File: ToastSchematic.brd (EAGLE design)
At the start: 90 x 75 mm, 83 parts, among them Q1 DMN63D8LDW, Q2 DMN63D8LDW, Q3 DMN63D8LDW, Q4 DMN63D8LDW, T1 BPX81, T2 BPX81, T3 BPX81, T4 BPX81, T5 BPX81, T6 BPX81, U3 DRV8839_DSS_12, U4 DRV8839_DSS_12

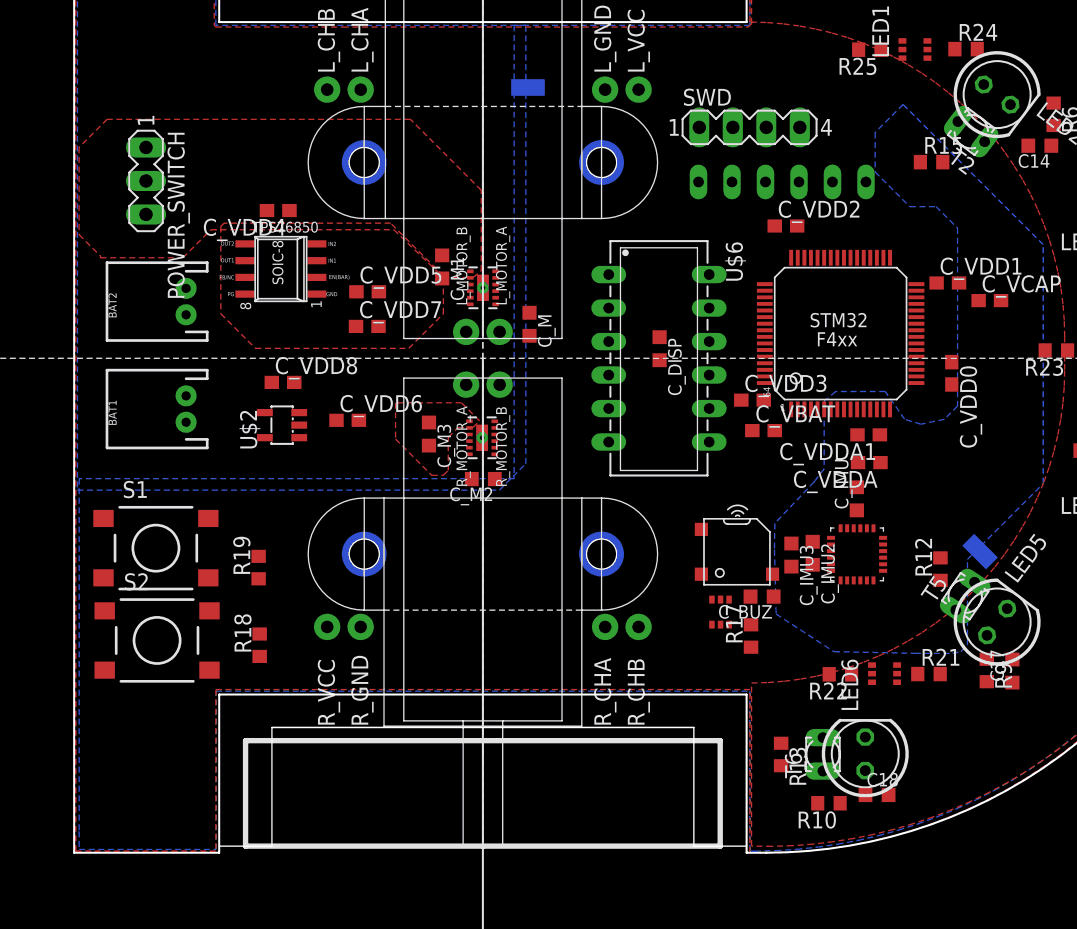
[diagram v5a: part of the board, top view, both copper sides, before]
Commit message: Added Ground Splitter
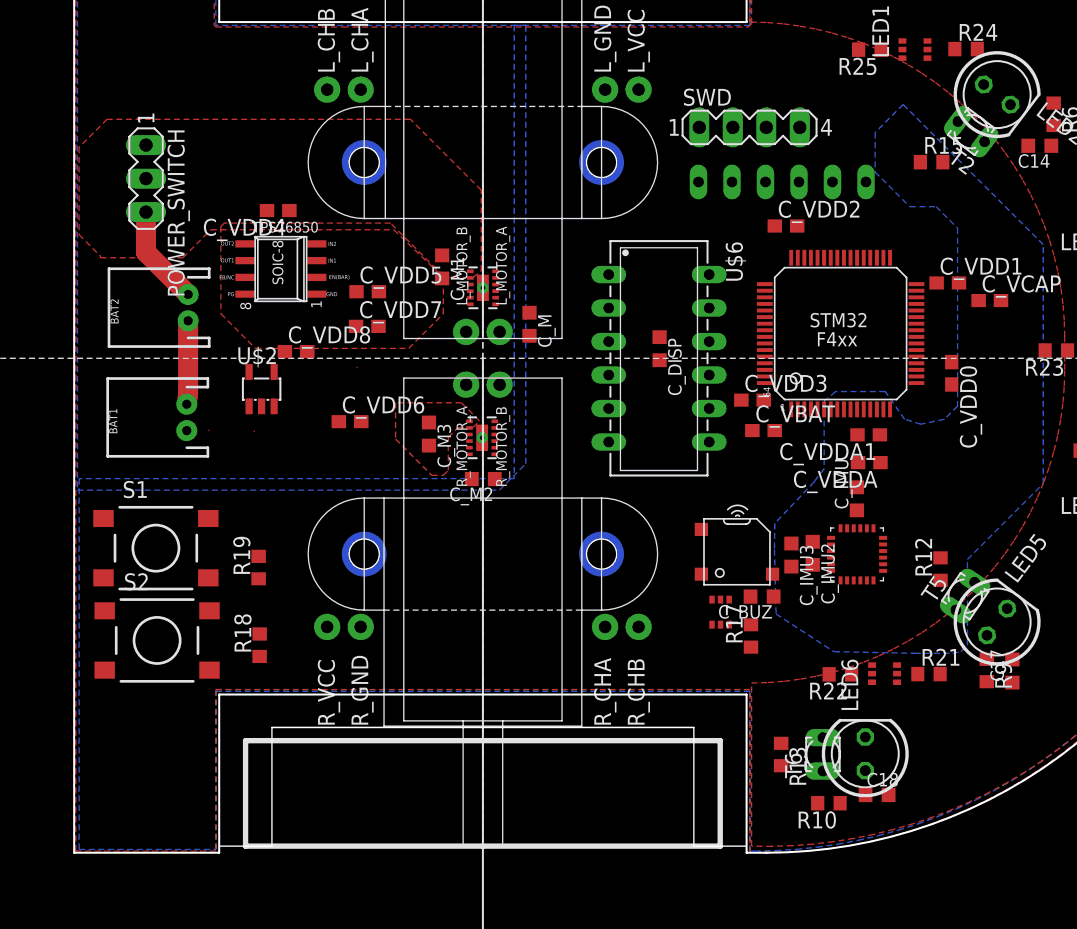
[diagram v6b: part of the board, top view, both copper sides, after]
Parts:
- removed SH1, SH2: SHORT-HT5, shorts-old:SHORT_TOP-50
- added U$5, U$8, U$9: SPLITTER, splitter:SPLITTER
- moved U$2 3.14 mm to (14.2, 35.2), turned to 0 degrees
- moved C_VDD8 2.54 mm to (16.8, 38.0)
- moved BAT1 0.64 mm to (8.54, 33.0)
- moved BAT2 0.48 mm to (8.64, 41.3)
- moved C_VDD6 0.20 mm to (20.9, 32.7)
- moved POWER_SWITCH 0.18 mm to (5.45, 51.1)
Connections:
- new net MGND: C_M.2, C_M2.2, U$9.2
- net AGND: now also U$8.2; no longer SH2.2
- net DGND: now also U$5.2; no longer SH1.2, SH2.1
- net GND: now also U$5.1, U$8.1, U$9.1; no longer C_M.2, C_M2.2, SH1.1
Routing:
- net N$2: track 0.00 -> 7.57 mm
- net N$1: track 0.00 -> 6.33 mm

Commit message: Get everything on cheap week
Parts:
- moved U$9 10.1 mm to (11.7, 34.5)
- moved R18 7.19 mm to (16.7, 22.4), turned to 270 degrees
- moved U$5 7.19 mm to (5.03, 37.0)
- moved C17 7.05 mm to (64.2, 12.5)
- moved U4 6.76 mm to (37.1, 40.0), turned to 180 degrees
- moved S1 6.40 mm to (7.38, 29.4), turned to 90 degrees
- moved U$8 5.25 mm to (12.2, 37.0)
- moved BAT1 5.06 mm to (7.78, 38.0)
- moved BAT2 4.22 mm to (7.70, 45.5)
- moved POWER_SWITCH 3.66 mm to (5.35, 54.8)
- moved S2 3.42 mm to (7.73, 19.2), turned to 180 degrees
- moved U$2 3.21 mm to (17.2, 36.4)
- moved R19 2.55 mm to (14.2, 24.2)
- moved C_IMU3 2.13 mm to (54.4, 24.7)
- moved R21 2.01 mm to (64.7, 15.6)
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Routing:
- net DGND: track 0.00 -> 245.6 mm
- net NRST: track 0.00 -> 72.8 mm, vias 0 -> 2
- net AGND: track 0.00 -> 64.4 mm, vias 0 -> 3
- net L_ENC_A: track 0.00 -> 37.0 mm
- net BUZZER: track 0.00 -> 31.6 mm, vias 0 -> 2
- net SCK: track 0.00 -> 29.3 mm
- net SWCLK: track 0.00 -> 28.3 mm
- net MGND: track 0.00 -> 27.9 mm
- net SWDIO: track 0.00 -> 21.9 mm, vias 0 -> 2
- net IR_DR: track 0.00 -> 20.2 mm
- net MOSI: track 0.00 -> 19.8 mm
- net IR_FR: track 0.00 -> 17.5 mm
- net IR_DL: track 0.00 -> 17.1 mm
- net REC_FL: track 0.00 -> 16.6 mm
- net IR_L: track 0.00 -> 15.9 mm
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
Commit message: Did more routing
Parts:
- moved U$8 55.4 mm to (66.8, 46.6), flipped to the bottom
- moved Q4 44.3 mm to (57.8, 61.7), turned to 270 degrees
- moved R17 43.2 mm to (56.0, 59.4), turned to 0 degrees
- moved SPK1 39.8 mm to (62.9, 60.5), turned to 180 degrees
- moved C_BUZ 39.7 mm to (59.0, 58.5), turned to 90 degrees
- moved U$5 33.5 mm to (34.4, 53.0), flipped to the bottom
- moved U$9 11.2 mm to (22.3, 31.2), flipped to the bottom
- moved C_VDD5 9.65 mm to (13.0, 45.4), turned to 90 degrees
- moved C_IMU3 9.00 mm to (59.9, 17.6), turned to 0 degrees
- moved C_IMU 8.13 mm to (55.8, 19.5), turned to 180 degrees
- moved C_M1 6.83 mm to (34.7, 44.8), turned to 90 degrees
- moved R19 6.50 mm to (14.0, 30.7)
- moved C_IMU2 6.41 mm to (59.9, 19.3), turned to 0 degrees
- moved C_M 5.49 mm to (37.0, 45.0), turned to 180 degrees
- moved C_VDD7 5.33 mm to (16.9, 40.6)
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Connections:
- net DGND: now also U$8.1
- net GND: no longer C_M1.2, C_M3.2, U$8.1, U3.13, U3.5, U3.6, U4.13, U4.5, U4.6
- net MGND: now also C_M1.2, C_M3.2, U3.13, U3.5, U3.6, U4.13, U4.5, U4.6
- net MOTOR_LEFT_1: now also U$4.L_MOTOR_B; no longer U$4.L_MOTOR_A
- net MOTOR_LEFT_2: now also U$4.L_MOTOR_A; no longer U$4.L_MOTOR_B
- net MOTOR_RIGHT_1: now also U$4.R_MOTOR_B; no longer U$4.R_MOTOR_A
- net MOTOR_RIGHT_2: now also U$4.R_MOTOR_A; no longer U$4.R_MOTOR_B
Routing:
- net DGND: track 245.6 -> 72.0 mm, vias 0 -> 23
- net +5V: track 0.00 -> 104.9 mm, vias 0 -> 5
- net BTN1: track 0.00 -> 76.4 mm, vias 0 -> 6
- net IR_R: track 0.00 -> 74.1 mm, vias 0 -> 8
- net M_R_B: track 0.00 -> 42.3 mm, vias 0 -> 5
- net M_R_F: track 0.00 -> 42.3 mm, vias 0 -> 4
- net L_ENC_B: track 0.00 -> 41.6 mm
- net +3V3: track 2.60 -> 40.5 mm
- net R_ENC_A: track 0.00 -> 33.0 mm, vias 0 -> 2
- net R_ENC_B: track 0.00 -> 31.6 mm, vias 0 -> 2
- net CS: track 0.00 -> 27.1 mm, vias 0 -> 2
- net BUZZER: track 31.6 -> 6.17 mm, vias 2 -> 0
- net M_L_B: track 0.00 -> 22.2 mm, vias 0 -> 2
- net M_L_F: track 0.00 -> 20.8 mm, vias 0 -> 2
- net INT: track 0.00 -> 17.4 mm, vias 0 -> 2
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- added copper zone on layer 16, net MGND
